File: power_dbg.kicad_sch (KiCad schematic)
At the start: 13 parts, among them J2 Conn_01x02, J3 Conn_ARM_JTAG_SWD_10, J6 USB_C_Receptacle_USB2.0, U2 AMS1117-33, U3 SRV05-4

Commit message: Save current state
We're thinking of adding a second stage "fine" tune, because... why not!
We're at ~$60 assembled for 5 boards, with everything optional filled
in, so adding 5x$1 to have the second range seems "free"?
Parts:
- J2: lcsc# (none) -> C2840336
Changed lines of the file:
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@@
+			)
+		)
+		(property "lcsc#" "C2840336"
+			(at 58.42 96.52 0)
+			(effects
+				(font
+					(size 1.27 1.27)
+				)
+				(hide yes)
 			)
 		)

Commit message: cleanup a bit
use red+green leds, sch on .100 grid, hook up more pins
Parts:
- R11: jlcbasic (none) -> basic
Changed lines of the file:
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@@
+			)
+		)
+		(property "jlcbasic" "basic"
+			(at 115.57 152.4 0)
+			(effects
+				(font
+					(size 1.27 1.27)
+				)
+				(hide yes)
 			)
 		)

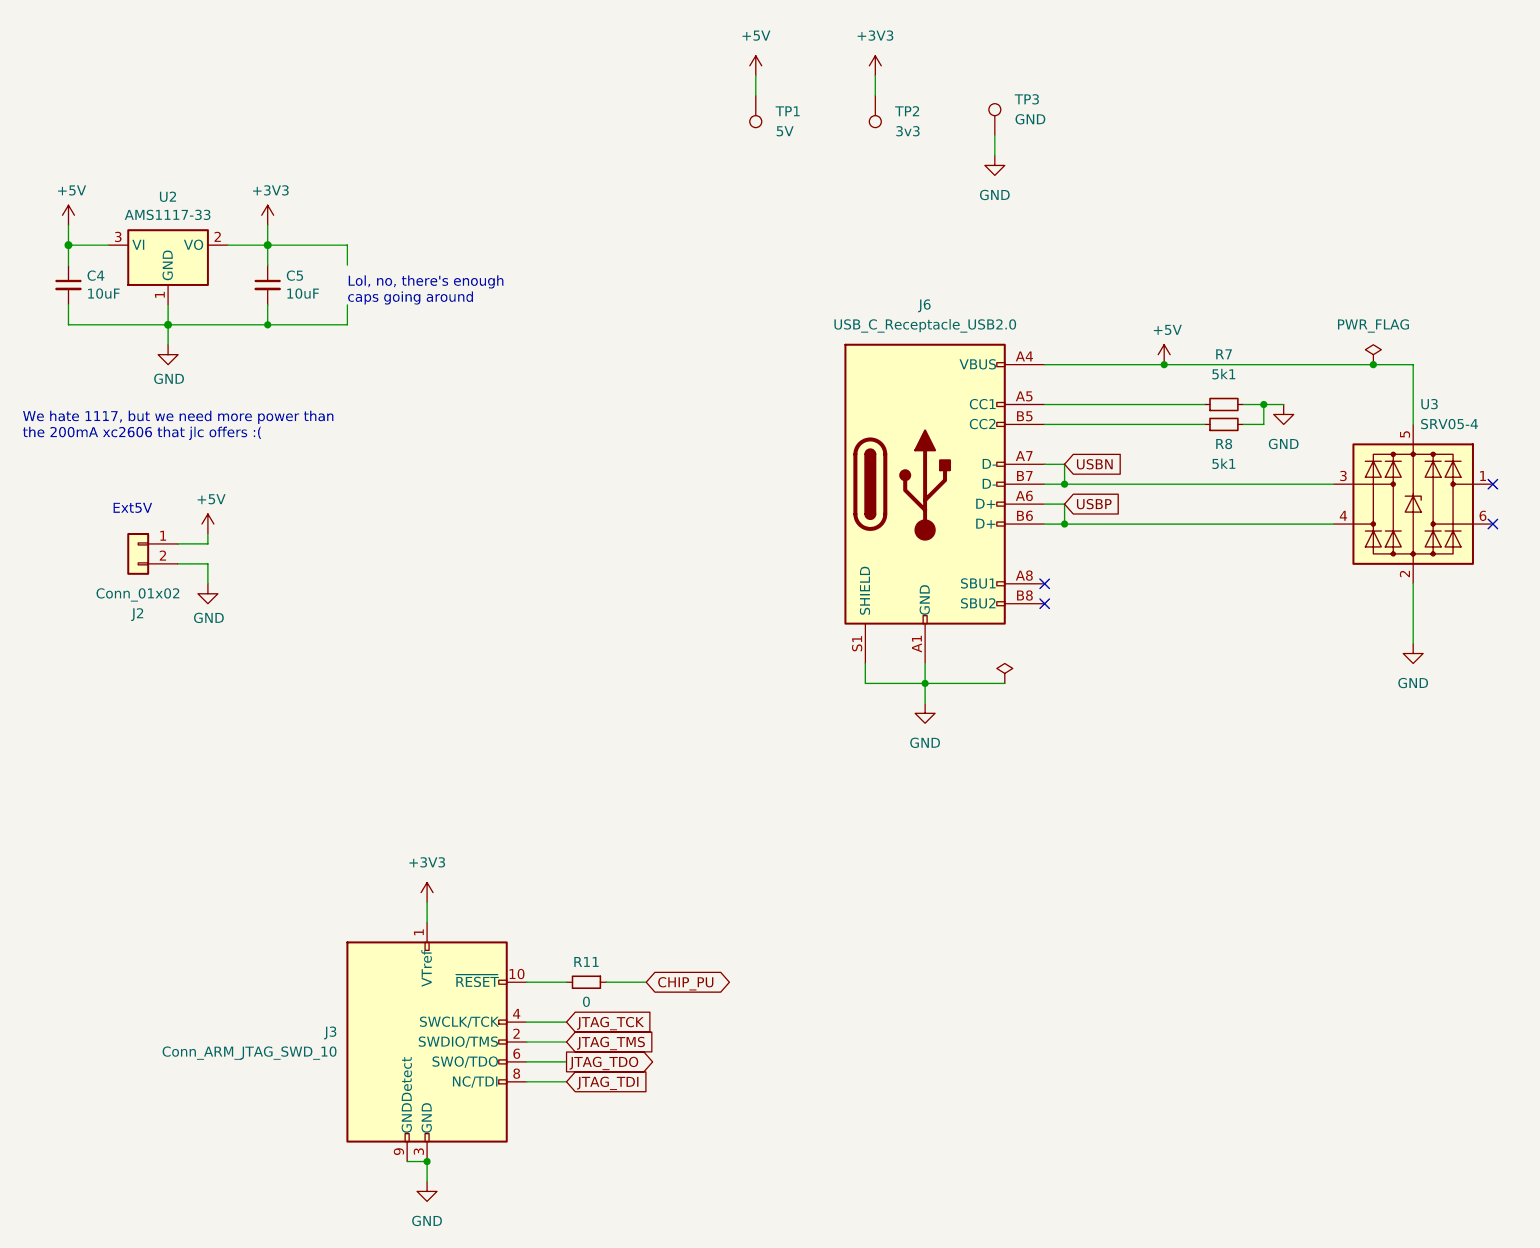
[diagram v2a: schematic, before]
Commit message: add the pwm method as an alternate impl
TODO: replace all resistors with 0805 so that precision _can_ be
soldered if desired
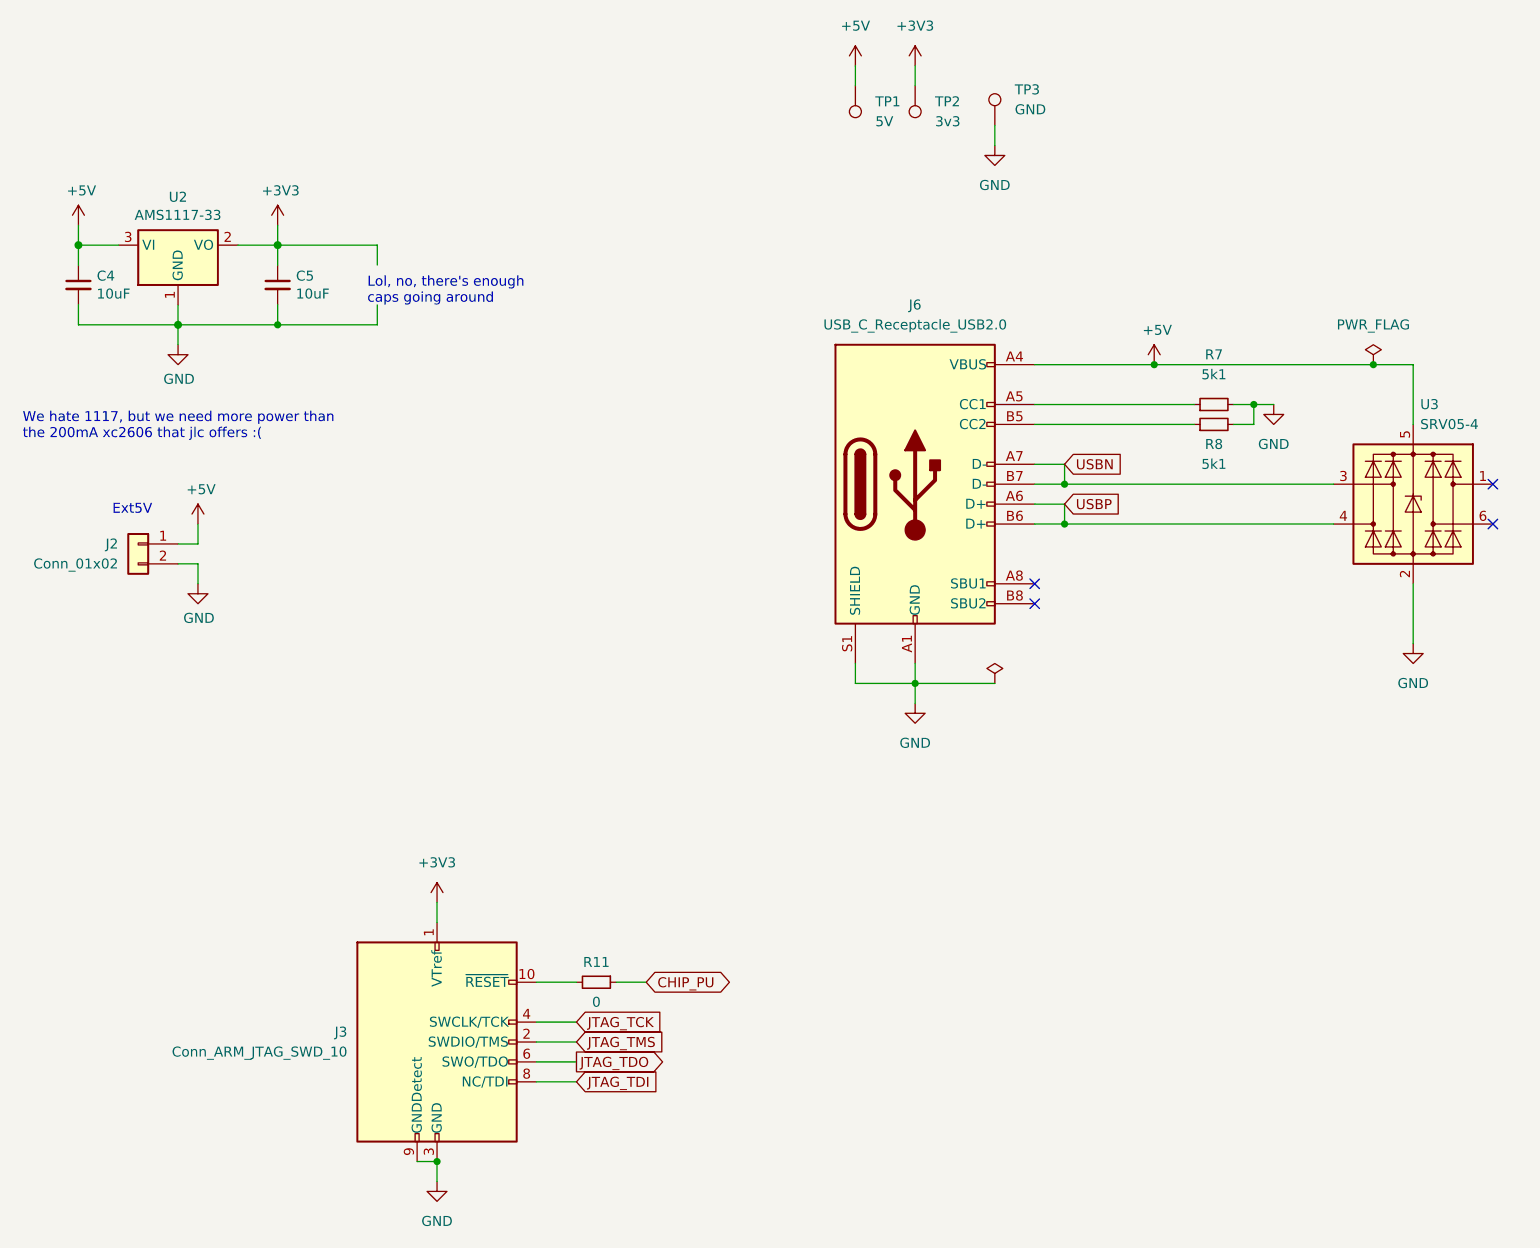
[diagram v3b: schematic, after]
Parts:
- J2: footprint Connector_Phoenix_MC:PhoenixContact_MC_1,5_2-G-3.5_1x02_P3.50mm_Horizontal -> Connector_Phoenix_MC:PhoenixContact_MC_1,5_2-G-3.81_1x02_P3.81mm_Horizontal; MPN (none) -> DB2ERC-3.81-2P-BK; lcsc# C2840336 -> C430323
- U2: jlcbasic (none) -> basic
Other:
- title: (none) -> LoadCell Faker
- moved on the sheet: C4, C5, J3, J6, R11, R7, R8, TP1, TP2, TP3, U2

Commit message: make a basic quick lib with jlc parts will  need extraction
Switch to 0805 for bridge resistors
switch to plain opto, we already have pulls and a fet.  (Could the other
one have directly pulled the resistor? (probably)
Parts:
- C4, C5: LCSC Part# (none) -> C15850; lcsc# C15850 -> (none)
- J2: LCSC Part# (none) -> C430323; lcsc# C430323 -> (none)
- J3: LCSC Part# (none) -> C6332249; lcsc# C6332249 -> (none)
- J6: LCSC Part# (none) -> C2927038; lcsc# C2927038 -> (none)
- R11: LCSC Part# (none) -> C21189; lcsc# C21189 -> (none)
- R7, R8: LCSC Part# (none) -> C23186; lcsc# C23186 -> (none)
- U2: LCSC Part# (none) -> C6186; lcsc# C6186 -> (none)
- U3: LCSC Part# (none) -> C7420376; lcsc# C7420376 -> (none)
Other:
- note added: "Dealon USB-TYPE-C-018 C2927038 0.04 G-Switch GT-USB-7010ASV C2988369 0.07 XKB U262-161N-4BVC11 C319148 0.21"
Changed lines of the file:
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@@
+		)
+	)
+	(text "Dealon USB-TYPE-C-018 C2927038 0.04\nG-Switch GT-USB-7010ASV C2988369 0.07\nXKB U262-161N-4BVC11 C319148  0.21"
+		(exclude_from_sim no)
+		(at 175.006 129.794 0)
+		(effects
+			(font
+				(size 1.27 1.27)
+			)
 		)
 	)
@@
 			)
 		)
-		(property "lcsc#" "C15850"
-			(at 76.2 63.5 0)
-			(effects
-				(font
-					(size 1.27 1.27)
-				)
-				(hide yes)
-			)
-		)
 		(property "jlc-basic" "1"
 			(at 76.2 63.5 0)
@@
 			)
 		)
+		(property "LCSC Part#" "C15850"
+			(at 76.2 63.5 0)
+			(effects
+				(font
+					(size 1.27 1.27)
+				)
+				(hide yes)
+			)
+		)
 		(pin "1"
 		)
@@
 			)
 		)
-		(property "lcsc#" "C15850"
-			(at 50.8 63.5 0)
-			(effects
-				(font
-					(size 1.27 1.27)
-				)
-				(hide yes)
-			)
-		)
 		(property "jlc-basic" "1"
 			(at 50.8 63.5 0)
@@
 			)
 		)
+		(property "LCSC Part#" "C15850"
+			(at 50.8 63.5 0)
+			(effects
+				(font
+					(size 1.27 1.27)
+				)
+				(hide yes)
+			)
+		)
 		(pin "1"
 		)
@@
 			)
 		)
-		(property "lcsc#" "C6332249"
-			(at 96.52 160.02 0)
-			(effects
-				(font
-					(size 1.27 1.27)
-				)
-				(hide yes)
-			)
-		)
 		(property "lcsc2#" ""
 			(at 96.52 160.02 0)
@@
 			)
 		)
+		(property "LCSC Part#" "C6332249"
+			(at 96.52 160.02 0)
+			(effects
+				(font
+					(size 1.27 1.27)
+				)
+				(hide yes)
+			)
+		)
 		(pin "2"
 		)
@@
 			)
 		)
-		(property "lcsc#" "C23186"
-			(at 195.58 81.28 0)
-			(effects
-				(font
-					(size 1.27 1.27)
-				)
-				(hide yes)
-			)
-		)
 		(property "MPN" "0603WAF5101T5E"
 			(at 195.58 81.28 0)
@@
 		)
 		(property "jlcbasic" "basic"
+			(at 195.58 81.28 0)
+			(effects
+				(font
+					(size 1.27 1.27)
+				)
+				(hide yes)
+			)
+		)
+		(property "LCSC Part#" "C23186"
 			(at 195.58 81.28 0)
 			(effects
@@
 			)
 		)
-		(property "lcsc#" "C430323"
-			(at 58.42 96.52 0)
-			(effects
-				(font
-					(size 1.27 1.27)
-				)
-				(hide yes)
-			)
-		)
 		(property "MPN" "DB2ERC-3.81-2P-BK"
 			(at 58.42 96.52 0)
@@
 			)
 		)
+		(property "LCSC Part#" "C430323"
+			(at 58.42 96.52 0)
+			(effects
+				(font
+					(size 1.27 1.27)
+				)
+				(hide yes)
+			)
+		)
 		(pin "2"
 		)
@@
 			)
 		)
-		(property "lcsc#" "C21189"
-			(at 116.84 152.4 0)
-			(effects
-				(font
-					(size 1.27 1.27)
-				)
-				(hide yes)
-			)
-		)
 		(property "jlcbasic" "basic"
 			(at 116.84 152.4 0)
@@
 			)
 		)
+		(property "LCSC Part#" "C21189"
+			(at 116.84 152.4 0)
+			(effects
+				(font
+					(size 1.27 1.27)
+				)
+				(hide yes)
+			)
+		)
 		(pin "1"
 		)
@@
 			)
 		)
-		(property "lcsc#" "C2927038"
-			(at 157.48 88.9 0)
-			(effects
-				(font
-					(size 1.27 1.27)
-				)
-				(hide yes)
-			)
-		)
 		(property "MPN" "USB-TYPE-C-018"
 			(at 157.48 88.9 0)
@@
 		)
 		(property "lcsc2#" ""
+			(at 157.48 88.9 0)
+			(effects
+				(font
+					(size 1.27 1.27)
+				)
+				(hide yes)
+			)
+		)
+		(property "LCSC Part#" "C2927038"
 			(at 157.48 88.9 0)
 			(effects
@@
 			)
 		)
-		(property "lcsc#" "C7420376"
-			(at 220.98 91.44 0)
-			(effects
-				(font
-					(size 1.27 1.27)
-				)
-				(hide yes)
-			)
-		)
 		(property "jlc-basic" "1"
 			(at 220.98 91.44 0)
@@
 			)
 		)
+		(property "LCSC Part#" "C7420376"
+			(at 220.98 91.44 0)
+			(effects
+				(font
+					(size 1.27 1.27)
+				)
+				(hide yes)
+			)
+		)
 		(pin "1"
 		)
@@
 			)
 		)
-		(property "lcsc#" "C23186"
-			(at 195.58 78.74 0)
-			(effects
-				(font
-					(size 1.27 1.27)
-				)
-				(hide yes)
-			)
-		)
 		(property "MPN" "0603WAF5101T5E"
 			(at 195.58 78.74 0)
@@
 			)
 		)
+		(property "LCSC Part#" "C23186"
+			(at 195.58 78.74 0)
+			(effects
+				(font
+					(size 1.27 1.27)
+				)
+				(hide yes)
+			)
+		)
 		(pin "1"
 		)
@@
 			)
 		)
-		(property "lcsc#" "C6186"
-			(at 63.5 58.42 0)
-			(effects
-				(font
-					(size 1.27 1.27)
-				)
-				(hide yes)
-			)
-		)
 		(property "jlcbasic" "basic"
 			(at 63.5 58.42 0)
 			(effects
+				(font
+					(size 1.27 1.27)
+				)
+				(hide yes)
+			)
+		)
+		(property "LCSC Part#" "C6186"
+			(at 63.5 58.42 0)
+			(effects

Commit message: add 3 OC outputs
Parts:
- C4, C5: jlcbasic (none) -> basic
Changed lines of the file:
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@@
 			)
 		)
-		(property "Description" ""
+		(property "Description" "Power symbol creates a global label with name \"+3V3\""
 			(at 157.48 35.56 0)
 			(effects
@@
 			)
 		)
-		(property "Description" ""
+		(property "Description" "Power symbol creates a global label with name \"+5V\""
 			(at 187.96 73.66 0)
 			(effects
@@
 			)
 		)
-		(property "Description" ""
+		(property "Description" "Unpolarized capacitor, small symbol"
 			(at 76.2 63.5 0)
 			(effects
@@
 		)
 		(property "LCSC Part#" "C15850"
+			(at 76.2 63.5 0)
+			(effects
+				(font
+					(size 1.27 1.27)
+				)
+				(hide yes)
+			)
+		)
+		(property "jlcbasic" "basic"
 			(at 76.2 63.5 0)
 			(effects
@@
 			)
 		)
-		(property "Description" ""
+		(property "Description" "test point"
 			(at 157.48 38.1 0)
 			(effects
@@
 			)
 		)
-		(property "Description" ""
+		(property "Description" "Unpolarized capacitor, small symbol"
 			(at 50.8 63.5 0)
 			(effects
@@
 			)
 		)
+		(property "jlcbasic" "basic"
+			(at 50.8 63.5 0)
+			(effects
+				(font
+					(size 1.27 1.27)
+				)
+				(hide yes)
+			)
+		)
 		(pin "1"
 		)
@@
 			)
 		)
-		(property "Description" ""
+		(property "Description" "Power symbol creates a global label with name \"+5V\""
 			(at 50.8 55.88 0)
 			(effects
@@
 			)
 		)
-		(property "Description" ""
+		(property "Description" "Power symbol creates a global label with name \"+5V\""
 			(at 66.04 93.98 0)
 			(effects
@@
 			)
 		)
-		(property "Description" ""
+		(property "Description" "Cortex Debug Connector, standard ARM Cortex-M SWD and JTAG interface"
 			(at 96.52 160.02 0)
 			(effects
@@
 			)
 		)
-		(property "Description" ""
+		(property "Description" "Resistor, small symbol"
 			(at 195.58 81.28 0)
 			(effects
@@
 			)
 		)
-		(property "Description" ""
+		(property "Description" "Resistor, small symbol"
 			(at 116.84 152.4 0)
 			(effects
@@
 			)
 		)
-		(property "Description" ""
+		(property "Description" "test point"
 			(at 167.64 43.18 0)
 			(effects
@@
 			)
 		)
-		(property "Description" ""
+		(property "Description" "Special symbol for telling ERC where power comes from"
 			(at 167.64 114.3 0)
 			(effects
@@
 			)
 		)
-		(property "Description" ""
+		(property "Description" "Power symbol creates a global label with name \"GND\" , ground"
 			(at 220.98 109.22 0)
 			(effects
@@
 			)
 		)
-		(property "Description" ""
+		(property "Description" "Power symbol creates a global label with name \"+3V3\""
 			(at 96.52 142.24 0)
 			(effects
@@
 			)
 		)
-		(property "Description" ""
+		(property "Description" "test point"
 			(at 149.86 38.1 0)
 			(effects
@@
 			)
 		)
-		(property "Description" ""
+		(property "Description" "Resistor, small symbol"
 			(at 195.58 78.74 0)
 			(effects
@@
 			)
 		)
-		(property "Description" ""
+		(property "Description" "Power symbol creates a global label with name \"GND\" , ground"
 			(at 157.48 116.84 0)
 			(effects
@@
 			)
 		)
-		(property "Description" ""
+		(property "Description" "Power symbol creates a global label with name \"GND\" , ground"
 			(at 63.5 71.12 0)
 			(effects
@@
 			)
 		)
-		(property "Description" ""
+		(property "Description" "Special symbol for telling ERC where power comes from"
 			(at 215.9 73.66 0)
 			(effects
@@
 			)
 		)
-		(property "Description" ""
+		(property "Description" "Power symbol creates a global label with name \"GND\" , ground"
 			(at 167.64 45.72 0)
 			(effects
@@
 			)
 		)
-		(property "Description" ""
+		(property "Description" "Power symbol creates a global label with name \"+3V3\""
 			(at 76.2 55.88 0)
 			(effects
@@
 			)
 		)
-		(property "Description" ""
+		(property "Description" "1A Low Dropout regulator, positive, 3.3V fixed output, SOT-223"
 			(at 63.5 58.42 0)
 			(effects
@@
 			)
 		)
-		(property "Description" ""
+		(property "Description" "Power symbol creates a global label with name \"+5V\""
 			(at 149.86 35.56 0)
 			(effects
@@
 			)
 		)
-		(property "Description" ""
+		(property "Description" "Power symbol creates a global label with name \"GND\" , ground"
 			(at 96.52 177.8 0)
 			(effects
@@
 			)
 		)
-		(property "Description" ""
+		(property "Description" "Power symbol creates a global label with name \"GND\" , ground"
 			(at 203.2 78.74 0)
 			(effects
@@
 			)
 		)
-		(property "Description" ""
+		(property "Description" "Power symbol creates a global label with name \"GND\" , ground"
 			(at 66.04 101.6 0)
 			(effects
